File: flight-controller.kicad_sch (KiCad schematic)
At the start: 0 parts

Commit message: Add STM32G474 to schematic
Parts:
- added C1: 4.7uF, symbol Device:C_Small
- added C2, C3, C4, C5: 100nF, symbol Device:C_Small
- added C6: 1uF, symbol Device:C_Small
- added C7: 10nF, symbol Device:C_Small
- added R1: 0, symbol Device:R_Small
- added U1: STM32G474RETx, Package_QFP:LQFP-64_10x10mm_P0.5mm, symbol MCU_ST_STM32G4:STM32G474RETx
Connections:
- new net: R1.1, U1.29 (VDDA)
- new net +3V3: C1.1, C2.1, C3.1, C4.1, C5.1, C6.1, C7.1, R1.2, U1.1 (VBAT), U1.16 (VDD), U1.32 (VDD), U1.48 (VDD), U1.64 (VDD)
- new net GND: C1.2, C2.2, C3.2, C4.2, C5.2, C6.2, C7.2, U1.15 (VSS), U1.27 (VSSA), U1.31 (VSS), U1.47 (VSS), U1.63 (VSS)

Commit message: Some schematic progress
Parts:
- added C9: 100nF, symbol Device:C_Small
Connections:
- net GND: now also C9.2; no longer C1.2, C2.2, C4.2, C5.2
- net SWDIO: now reaches U1.49 (PA13)
- net OSCX_IN: now reaches U1.5 (PF0)
- net SWCLK: now reaches U1.50 (PA14)
- net OSCX_OUT: now reaches U1.6 (PF1)
- net NRST: now reaches U1.7 (PG10)
- net NRST: now also C9.1
- new net: C1.2, C2.2, C4.2, C5.2
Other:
- added sheet MCU-Peripherals (MCU-Peripherals.kicad_sch)
- note added: "MCU"
- moved on the sheet: C1, C2, C3, C4, C5, C6, C7, R1, U1

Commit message: Decent progress, started USB
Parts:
- added C11: 1 uF, symbol Device:C_Small
- added C12: 100 nF, symbol Device:C_Small
- added R5: 0, symbol Device:R_Small
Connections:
- net GND: now also C11.2, C12.2
- net at U1.28 (VREF+): now also C11.1, C12.1, R5.2
- net at R1.1, U1.29 (VDDA): now also R5.1
- net BOOT0: now reaches U1.61 (PB8)
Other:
- moved on the sheet: C1, C2, C3, C4, C5, C9

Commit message: Further schematic progress
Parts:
- added R3: 0, symbol Device:R_Small
- added R4: 10k, symbol Device:R_Small
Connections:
- net GND: now also R4.2
- net QSPI_NCS: now reaches U1.14 (PA2)
- net at U1.17 (PA3): now also R3.1
- net CAN_STBY: now reaches U1.2 (PC13)
- net CAN_STBY: now also R4.1
- net QSPI_IO3: now reaches U1.20 (PA6)
- net QSPI_IO2: now reaches U1.21 (PA7)
- net INT1: now reaches U1.22 (PC4)
- net INT2: now reaches U1.23 (PC5)
- net QSPI_IO1: now reaches U1.24 (PB0)
- net QSPI_IO0: now reaches U1.25 (PB1)
- net SPI2_NSS: now reaches U1.34 (PB12)
- net SPI2_SCK: now reaches U1.35 (PB13)
- net SPI2_MISO: now reaches U1.36 (PB14)
- net SPI2_MOSI: now reaches U1.37 (PB15)
- net D-: now reaches U1.45 (PA11)
- net D+: now reaches U1.46 (PA12)
- net FDCAN2_RX: now reaches U1.58 (PB5)
- net FDCAN2_TX: now reaches U1.59 (PB6)
- new net QSPI_SCK: R3.2
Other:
- added sheet Sensors (IMU.kicad_sch)
- moved on the sheet: C1, C11, C12, C2, C3, C4, C5, C6, C7, C9, R1, R5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

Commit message: Completed Schematic
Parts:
- added C26: 100 nF, symbol Device:C_Small
- added R10, R12: 10k, symbol Device:R
- added R13: 100k, symbol Device:R
- added R14: 150k, symbol Device:R
- added TP1, TP10, TP11, TP12, TP2, TP3, TP4, TP5, TP6, TP7, TP8, TP9: TestPoint, symbol Connector:TestPoint
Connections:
- net +3V3: now also TP12.1; no longer C6.1, C7.1
- net GND: now also C1.2, C2.2, C4.2, C5.2, C26.2, R12.2, R14.2, TP10.1
- net NRST: now also TP1.1
- net 5V_SENSE_ADC: now reaches U1.12 (PA0)
- net 5V_SENSE_ADC: now also C26.1, R10.2, R12.1, TP6.1
- net at R1.1, R5.1, U1.29 (VDDA): now also C6.1, C7.1
- net UART3_TX: now reaches U1.30 (PB10)
- net UART3_TX: now also TP2.1
- net UART3_RX: now reaches U1.33 (PB11)
- net UART3_RX: now also TP3.1
- net at U1.43 (PA9): now also R13.2, R14.1
- net I_SENSE_ADC: now reaches U1.8 (PC0)
- net I_SENSE_ADC: now also TP4.1
- net TEMP_SENSE_ADC: now reaches U1.9 (PC1)
- net TEMP_SENSE_ADC: now also TP5.1
- new net +5V_LOAD: R10.1, TP8.1
- new net +5V_SYS: TP7.1
- new net EXT_5V: TP11.1
- new net EXT_5V_RAW: TP9.1
- new net USB_5V: R13.1
- no-connect marks 0 -> 23
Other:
- added sheet Power-Architecture (power-architecture.kicad_sch)
- moved on the sheet: C1, C11, C12, C2, C3, C4, C5, R1, R4

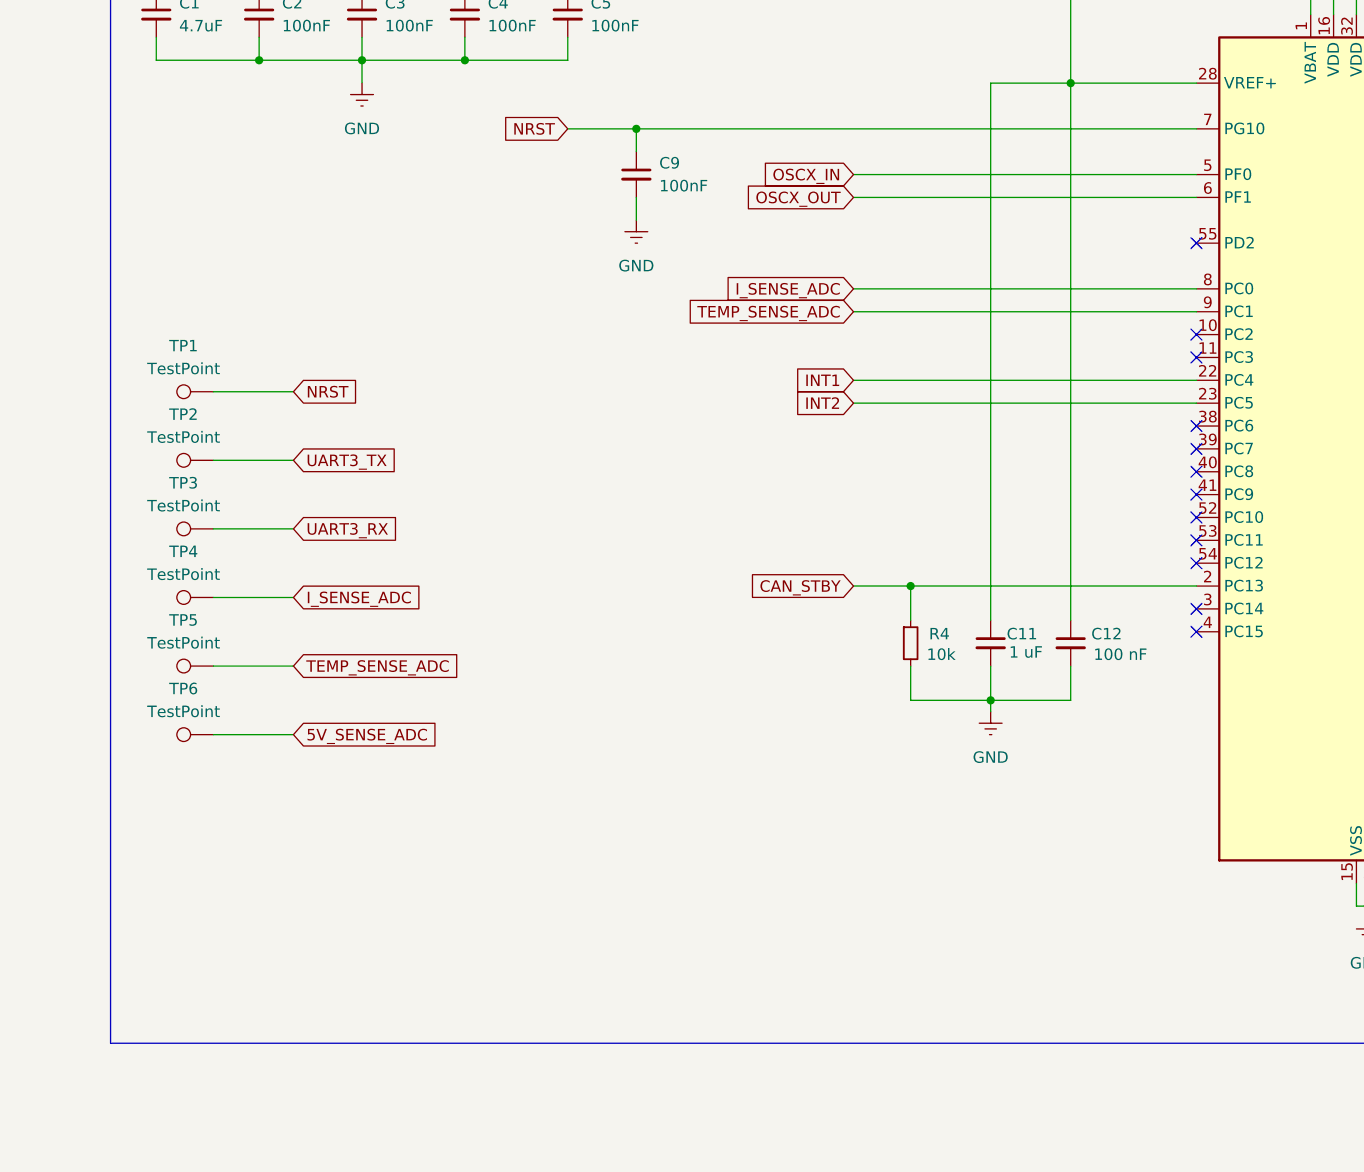
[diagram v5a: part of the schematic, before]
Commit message: PCB Layout Component placement progress
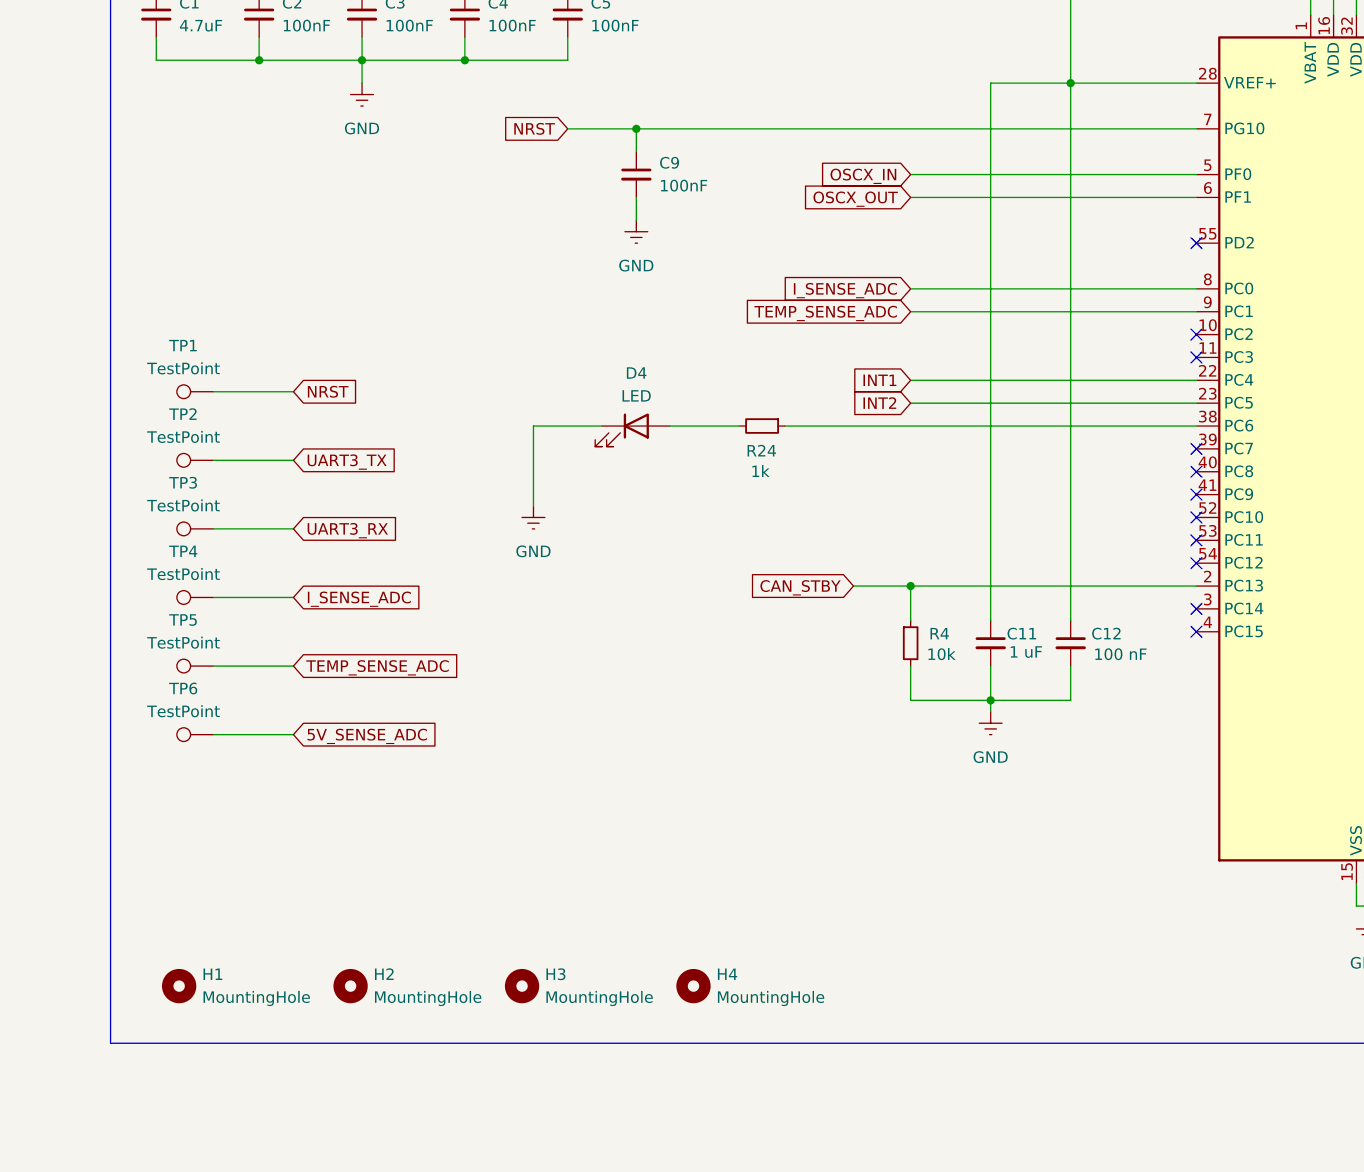
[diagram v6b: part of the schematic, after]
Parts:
- added D4: LED, LED_SMD:LED_0603_1608Metric, symbol Device:LED
- added H1, H2, H3, H4: MountingHole, MountingHole:MountingHole_3.2mm_M3_Pad_Via, symbol Mechanical:MountingHole
- added R24: 1k, Resistor_SMD:R_0603_1608Metric, symbol Device:R_Small
- C1: footprint (none) -> Capacitor_SMD:C_0805_2012Metric
- C11, C12, C2, C26, C3, C4, C5, C6, C7, C9: footprint (none) -> Capacitor_SMD:C_0603_1608Metric
- R1, R10, R12, R13, R14, R3, R4, R5: footprint (none) -> Resistor_SMD:R_0603_1608Metric
- TP1, TP10, TP11, TP12, TP2, TP3, TP4, TP5, TP6, TP7, TP8, TP9: footprint (none) -> TestPoint:TestPoint_Pad_D1.0mm
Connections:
- net GND: now also D4.1 (K)
- net at U1.38 (PC6): now also R24.1
- new net: D4.2 (A), R24.2
- no-connect marks 23 -> 22

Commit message: Finished PCB Component Placement
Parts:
- added TP13, TP14, TP15: TestPoint, TestPoint:TestPoint_Pad_D1.0mm, symbol Connector:TestPoint
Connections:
- net GND: now also TP13.1, TP14.1, TP15.1
